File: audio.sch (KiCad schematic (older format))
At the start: 80 parts, among them CN1 LEFT_JOY, CN2 RIGHT_JOY, CN3 RIGHT, CN4 LEFT, Q301 2N3906, Q321 MPF102, Q331 MPF102, U14 LF347, U15 74LS157, U3 PAULA, U38 MC1488

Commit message: Add video power
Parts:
- R401, R408: footprint (none) -> Resistor_THT:R_Axial_DIN0309_L9.0mm_D3.2mm_P15.24mm_Horizontal
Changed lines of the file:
@@
 F 0 "R401" V 6530 1560 50  0000 L CNN
 F 1 "4.7" V 6625 1595 50  0000 L CNN
-F 2 "" V 6555 1660 50  0001 C CNN
+F 2 "Resistor_THT:R_Axial_DIN0309_L9.0mm_D3.2mm_P15.24mm_Horizontal" V 6555 1660 50  0001 C CNN
 F 3 "~" H 6625 1660 50  0001 C CNN
 	1    6625 1660
@@
 F 0 "R408" V 6530 3790 50  0000 L CNN
 F 1 "4.7" V 6625 3825 50  0000 L CNN
-F 2 "" V 6555 3890 50  0001 C CNN
+F 2 "Resistor_THT:R_Axial_DIN0309_L9.0mm_D3.2mm_P15.24mm_Horizontal" V 6555 3890 50  0001 C CNN
 F 3 "~" H 6625 3890 50  0001 C CNN
 	1    6625 3890
@@
 Wire Wire Line
 	5995 5030 7280 5030
-Wire Bus Line
-	1955 4305 1955 4505
-Wire Bus Line
-	1955 6355 1955 7055
-Wire Bus Line
-	1955 4705 1955 6205
 Text Label 1580 4305 0    50   ~ 0
 ipl[0..2]
@@
 Text Label 2130 4605 0    50   ~ 0
 ipl0
+Wire Bus Line
+	1955 4305 1955 4505
+Wire Bus Line
+	1955 6355 1955 7055
+Wire Bus Line
+	1955 4705 1955 6205
 $EndSCHEMATC

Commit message: Add expansion bus
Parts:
- added C3, C301, C302, C305: 330n, symbol Device:C
- added C303, C304: 22u, symbol Device:CP1
- added C306: 10u, symbol Device:CP1
- added C307: 1000u, symbol Device:CP1
- added R301, R302: 10, Raemixx500:R_Axial_DIN0309_L9.0mm_D3.2mm_P12.70mm_Horizontal, symbol Device:R
- added R303, R304: 1k, Raemixx500:R_Axial_DIN0309_L9.0mm_D3.2mm_P12.70mm_Horizontal, symbol Device:R
- added R309: 10, symbol Device:R
- added unit 5 of U14
- added unit 2 of U3
- R305: footprint (none) -> Raemixx500:R_Axial_DIN0309_L9.0mm_D3.2mm_P12.70mm_Horizontal
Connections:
- net labels added: +VDC, -VDC
- net labels removed: VAA
- wire segments 426 -> 477
- no-connect marks 3 -> 4
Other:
- note added: "+VDC (+AV\non original\nschematics) is\npicked up here"
- note added: "-VDC (-AV\non original\nschematics) is\npicked up here"
- note added: "AUDIO POWER"
- note added: "Audio Power\nSupply (+AV/-AV)"
- note added: "PAULA POWER"
- note added: "VAC (VREF\non original\nschematics) is\npicked up here"
- note added: "Vref"
- note removed: "AVref"
- note removed: "Audio Power Supply"
- moved on the sheet: R308, U38A

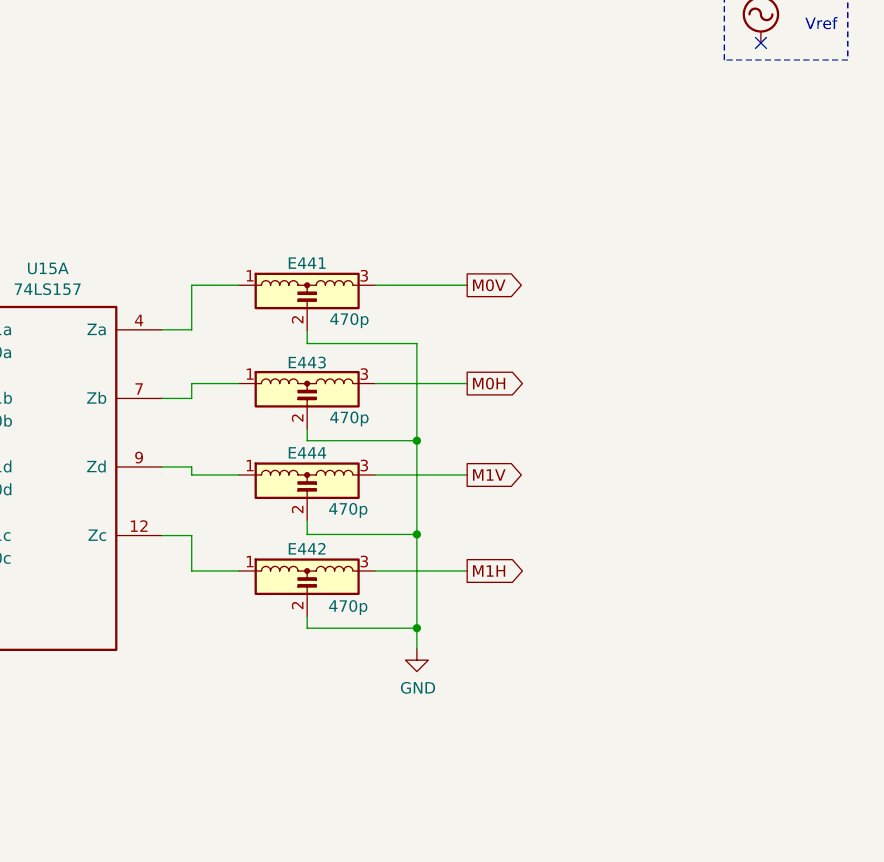
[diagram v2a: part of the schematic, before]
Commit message: Add power & decoupling, not yet complete
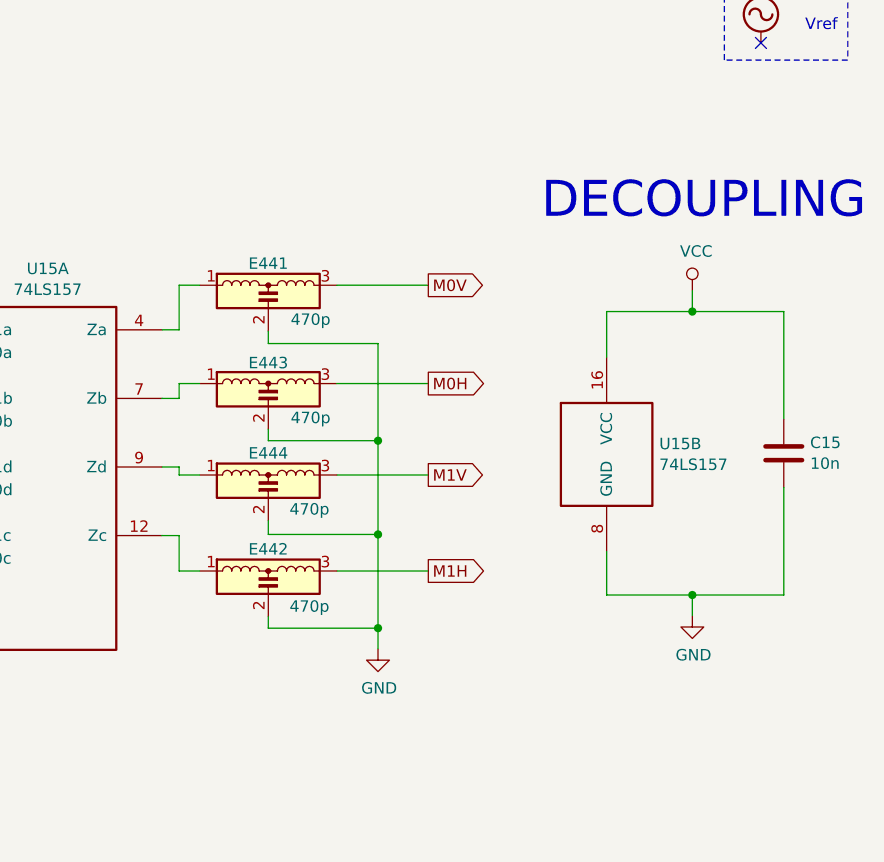
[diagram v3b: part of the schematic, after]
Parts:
- added C15: 10n, symbol Device:C
- added unit 2 of U15
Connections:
- net GND: now also C15.2, U15.8 (GND)
- net VCC: now also C15.1, U15.16 (VCC)
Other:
- note added: "DECOUPLING"
- moved on the sheet: E441, E442, E443, E444
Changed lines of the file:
@@
 $Descr A3 16535 11693
 encoding utf-8
-Sheet 5 11
+Sheet 5 12
 Title "Rämixx500"
 Date "2019-04-16"
@@
 L Device:EMI_Filter_LCL E441
 U 1 1 5D569D5D
-P 13590 2680
-F 0 "E441" H 13590 2875 50  0000 C CNN
-F 1 "470p" H 13775 2630 50  0000 C CNN
-F 2 "" V 13590 2680 50  0001 C CNN
-F 3 "http://www.murata.com/~/media/webrenewal/support/library/catalog/products/emc/emifil/c31e.ashx?la=en-gb" V 13590 2680 50  0001 C CNN
-	1    13590 2680
+P 13420 2680
+F 0 "E441" H 13420 2875 50  0000 C CNN
+F 1 "470p" H 13605 2630 50  0000 C CNN
+F 2 "" V 13420 2680 50  0001 C CNN
+F 3 "http://www.murata.com/~/media/webrenewal/support/library/catalog/products/emc/emifil/c31e.ashx?la=en-gb" V 13420 2680 50  0001 C CNN
+	1    13420 2680
 	1    0    0    -1
 $EndComp
@@
 L Device:EMI_Filter_LCL E443
 U 1 1 5D569D63
-P 13590 3110
-F 0 "E443" H 13590 3300 50  0000 C CNN
-F 1 "470p" H 13775 3060 50  0000 C CNN
-F 2 "" V 13590 3110 50  0001 C CNN
-F 3 "http://www.murata.com/~/media/webrenewal/support/library/catalog/products/emc/emifil/c31e.ashx?la=en-gb" V 13590 3110 50  0001 C CNN
-	1    13590 3110
+P 13420 3110
+F 0 "E443" H 13420 3300 50  0000 C CNN
+F 1 "470p" H 13605 3060 50  0000 C CNN
+F 2 "" V 13420 3110 50  0001 C CNN
+F 3 "http://www.murata.com/~/media/webrenewal/support/library/catalog/products/emc/emifil/c31e.ashx?la=en-gb" V 13420 3110 50  0001 C CNN
+	1    13420 3110
 	1    0    0    -1
 $EndComp
@@
 L Device:EMI_Filter_LCL E444
 U 1 1 5D569D69
-P 13590 3510
-F 0 "E444" H 13590 3705 50  0000 C CNN
-F 1 "470p" H 13770 3460 50  0000 C CNN
-F 2 "" V 13590 3510 50  0001 C CNN
-F 3 "http://www.murata.com/~/media/webrenewal/support/library/catalog/products/emc/emifil/c31e.ashx?la=en-gb" V 13590 3510 50  0001 C CNN
-	1    13590 3510
+P 13420 3510
+F 0 "E444" H 13420 3705 50  0000 C CNN
+F 1 "470p" H 13600 3460 50  0000 C CNN
+F 2 "" V 13420 3510 50  0001 C CNN
+F 3 "http://www.murata.com/~/media/webrenewal/support/library/catalog/products/emc/emifil/c31e.ashx?la=en-gb" V 13420 3510 50  0001 C CNN
+	1    13420 3510
 	1    0    0    -1
 $EndComp
@@
 L Device:EMI_Filter_LCL E442
 U 1 1 5D569D6F
-P 13590 3930
-F 0 "E442" H 13590 4125 50  0000 C CNN
-F 1 "470p" H 13770 3875 50  0000 C CNN
-F 2 "" V 13590 3930 50  0001 C CNN
-F 3 "http://www.murata.com/~/media/webrenewal/support/library/catalog/products/emc/emifil/c31e.ashx?la=en-gb" V 13590 3930 50  0001 C CNN
-	1    13590 3930
-	1    0    0    -1
-$EndComp
-Wire Wire Line
-	13890 2580 14290 2580
-Wire Wire Line
-	13590 2780 13590 2835
-Wire Wire Line
-	13590 2835 14070 2835
-Wire Wire Line
-	14070 2835 14070 3260
-Wire Wire Line
-	13590 3210 13590 3260
-Wire Wire Line
-	13590 3260 14070 3260
-Connection ~ 14070 3260
-Wire Wire Line
-	14070 3260 14070 3670
-Wire Wire Line
-	13590 3610 13590 3670
-Wire Wire Line
-	13590 3670 14070 3670
-Connection ~ 14070 3670
-Wire Wire Line
-	14070 3670 14070 4080
-Wire Wire Line
-	13590 4030 13590 4080
-Wire Wire Line
-	13590 4080 14070 4080
-Connection ~ 14070 4080
-Wire Wire Line
-	14070 4080 14070 4170
+P 13420 3930
+F 0 "E442" H 13420 4125 50  0000 C CNN
+F 1 "470p" H 13600 3875 50  0000 C CNN
+F 2 "" V 13420 3930 50  0001 C CNN
+F 3 "http://www.murata.com/~/media/webrenewal/support/library/catalog/products/emc/emifil/c31e.ashx?la=en-gb" V 13420 3930 50  0001 C CNN
+	1    13420 3930
+	1    0    0    -1
+$EndComp
+Wire Wire Line
+	13720 2580 14120 2580
+Wire Wire Line
+	13420 2780 13420 2835
+Wire Wire Line
+	13420 2835 13900 2835
+Wire Wire Line
+	13900 2835 13900 3260
+Wire Wire Line
+	13420 3210 13420 3260
+Wire Wire Line
+	13420 3260 13900 3260
+Connection ~ 13900 3260
+Wire Wire Line
+	13900 3260 13900 3670
+Wire Wire Line
+	13420 3610 13420 3670
+Wire Wire Line
+	13420 3670 13900 3670
+Connection ~ 13900 3670
+Wire Wire Line
+	13900 3670 13900 4080
+Wire Wire Line
+	13420 4030 13420 4080
+Wire Wire Line
+	13420 4080 13900 4080
+Connection ~ 13900 4080
+Wire Wire Line
+	13900 4080 13900 4170
 $Comp
 L power:GND #PWR0141
 U 1 1 5D569D94
-P 14070 4170
-F 0 "#PWR0141" H 14070 3920 50  0001 C CNN
-F 1 "GND" H 14075 3997 50  0000 C CNN
-F 2 "" H 14070 4170 50  0001 C CNN
-F 3 "" H 14070 4170 50  0001 C CNN
-	1    14070 4170
-	1    0    0    -1
-$EndComp
-Wire Wire Line
-	12955 3075 13085 3075
-Wire Wire Line
-	13085 3075 13085 3010
-Wire Wire Line
-	13085 3010 13290 3010
-Wire Wire Line
-	12955 2775 13085 2775
-Wire Wire Line
-	13085 2775 13085 2580
-Wire Wire Line
-	13085 2580 13290 2580
-Wire Wire Line
-	12955 3375 13085 3375
-Wire Wire Line
-	13085 3375 13085 3410
-Wire Wire Line
-	13085 3410 13290 3410
-Wire Wire Line
-	12955 3675 13085 3675
-Wire Wire Line
-	13085 3675 13085 3830
-Wire Wire Line
-	13085 3830 13290 3830
-Text GLabel 14290 2580 2    50   Output ~ 0
+P 13900 4170
+F 0 "#PWR0141" H 13900 3920 50  0001 C CNN
+F 1 "GND" H 13905 3997 50  0000 C CNN
+F 2 "" H 13900 4170 50  0001 C CNN
+F 3 "" H 13900 4170 50  0001 C CNN
+	1    13900 4170
+	1    0    0    -1
+$EndComp
+Wire Wire Line
+	12955 3075 13030 3075
+Wire Wire Line
+	13030 3075 13030 3010
+Wire Wire Line
+	13030 3010 13120 3010
+Wire Wire Line
+	12955 2775 13030 2775
+Wire Wire Line
+	13030 2775 13030 2580
+Wire Wire Line
+	13030 2580 13120 2580
+Wire Wire Line
+	12955 3375 13030 3375
+Wire Wire Line
+	13030 3375 13030 3410
+Wire Wire Line
+	13030 3410 13120 3410
+Wire Wire Line
+	12955 3675 13030 3675
+Wire Wire Line
+	13030 3675 13030 3830
+Wire Wire Line
+	13030 3830 13120 3830
+Text GLabel 14120 2580 2    50   Output ~ 0
 M0V
 Wire Wire Line
-	13890 3010 14290 3010
-Text GLabel 14290 3010 2    50   Output ~ 0
+	13720 3010 14120 3010
+Text GLabel 14120 3010 2    50   Output ~ 0
 M0H
 Wire Wire Line
-	13890 3410 14290 3410
-Text GLabel 14290 3410 2    50   Output ~ 0
+	13720 3410 14120 3410
+Text GLabel 14120 3410 2    50   Output ~ 0
 M1V
 Wire Wire Line
-	13890 3830 14290 3830
-Text GLabel 14290 3830 2    50   Output ~ 0
+	13720 3830 14120 3830
+Text GLabel 14120 3830 2    50   Output ~ 0
 M1H
 $Comp
@@
 Text Notes 525  11075 0    315  ~ 0
 AUDIO POWER
+$Comp
+L 74ls157:74LS157 U15
+U 2 1 5EC4854E
+P 14900 3345
+F 0 "U15" H 15130 3416 50  0000 L CNN
+F 1 "74LS157" H 15130 3325 50  0000 L CNN
+F 2 "Package_DIP:DIP-16_W7.62mm_Socket_LongPads" H 14900 3345 50  0001 C CNN
+F 3 "http://www.ti.com/lit/gpn/sn74LS157" H 14900 3345 50  0001 C CNN
+	2    14900 3345
+	1    0    0    -1
+$EndComp
+$Comp
+L Device:C C15
+U 1 1 5EC8858D
+P 15675 3315
+F 0 "C15" H 15790 3361 50  0000 L CNN
+F 1 "10n" H 15790 3270 50  0000 L CNN
+F 2 "" H 15713 3165 50  0001 C CNN
+F 3 "~" H 15675 3315 50  0001 C CNN
+	1    15675 3315
+	1    0    0    -1
+$EndComp
+Wire Wire Line
+	14900 2895 14900 2695
+Wire Wire Line
+	14900 2695 15275 2695
+Wire Wire Line
+	15675 2695 15675 3165
+Wire Wire Line
+	15675 3465 15675 3935
+Wire Wire Line
+	15675 3935 15275 3935
+Wire Wire Line
+	14900 3935 14900 3745
+Wire Wire Line
+	15275 3935 15275 4025
+$Comp
+L power:GND #PWR0222
+U 1 1 5ED09E51
+P 15275 4025
+F 0 "#PWR0222" H 15275 3775 50  0001 C CNN
+F 1 "GND" H 15280 3852 50  0000 C CNN
+F 2 "" H 15275 4025 50  0001 C CNN
+F 3 "" H 15275 4025 50  0001 C CNN
+	1    15275 4025
+	1    0    0    -1
+$EndComp
+Connection ~ 15275 3935
+Wire Wire Line
+	15275 3935 14900 3935
+$Comp
+L power:VCC #PWR0223
+U 1 1 5ED4B558
+P 15275 2605
+F 0 "#PWR0223" H 15275 2455 50  0001 C CNN
+F 1 "VCC" H 15292 2778 50  0000 C CNN
+F 2 "" H 15275 2605 50  0001 C CNN
+F 3 "" H 15275 2605 50  0001 C CNN
+	1    15275 2605
+	1    0    0    -1
+$EndComp
+Wire Wire Line
+	15275 2605 15275 2695
+Connection ~ 15275 2695
+Wire Wire Line
+	15275 2695 15675 2695
 Wire Bus Line
 	1955 4305 1955 4505
@@
 Wire Bus Line
 	1955 4705 1955 6205
+Text Notes 16035 2305 2    157  ~ 0
+DECOUPLING
 $EndSCHEMATC

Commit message: Add RTC
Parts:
- C303, C304: footprint (none) -> Capacitor_THT:CP_Radial_D5.0mm_P2.00mm
- C306, C307, C324, C334: footprint (none) -> Capacitor_THT:CP_Radial_D8.0mm_P5.00mm
- CN3: footprint (none) -> w_conn_av:rca_red
- CN4: footprint (none) -> w_conn_av:rca_white
- JP10A1, JP10B1: footprint Jumper:SolderJumper-2_P1.3mm_Bridged_RoundedPad1.0x1.5mm -> Raemixx500:Jumper2-Bridged
- JP8: footprint (none) -> Raemixx500:Jumper3-Bridged23
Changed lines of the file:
@@
 $Descr A3 16535 11693
 encoding utf-8
-Sheet 5 12
+Sheet 5 13
 Title "Rämixx500"
 Date "2019-04-16"
@@
 F 0 "JP8" V 5645 2507 50  0000 L CNN
 F 1 "Jumper_3_Bridged23" V 5690 2507 50  0001 L CNN
-F 2 "" H 5645 2440 50  0001 C CNN
+F 2 "Raemixx500:Jumper3-Bridged23" H 5645 2440 50  0001 C CNN
 F 3 "~" H 5645 2440 50  0001 C CNN
 	1    5645 2440
@@
 F 0 "C324" V 10525 8860 50  0000 C CNN
 F 1 "22u" V 10405 8885 50  0000 C CNN
-F 2 "" H 10475 9035 50  0001 C CNN
+F 2 "Capacitor_THT:CP_Radial_D8.0mm_P5.00mm" H 10475 9035 50  0001 C CNN
 F 3 "~" H 10475 9035 50  0001 C CNN
 	1    10475 9035
@@
 F 0 "CN4" H 12965 8891 50  0000 L CNN
 F 1 "LEFT" H 12965 8800 50  0000 L CNN
-F 2 "" H 12865 8915 50  0001 C CNN
+F 2 "w_conn_av:rca_white" H 12865 8915 50  0001 C CNN
 F 3 " ~" H 12865 8915 50  0001 C CNN
 	1    12865 8915
@@
 F 0 "C334" V 10525 7065 50  0000 C CNN
 F 1 "22u" V 10405 7090 50  0000 C CNN
-F 2 "" H 10475 7240 50  0001 C CNN
+F 2 "Capacitor_THT:CP_Radial_D8.0mm_P5.00mm" H 10475 7240 50  0001 C CNN
 F 3 "~" H 10475 7240 50  0001 C CNN
 	1    10475 7240
@@
 F 0 "CN3" H 12964 7096 50  0000 L CNN
 F 1 "RIGHT" H 12964 7005 50  0000 L CNN
-F 2 "" H 12865 7120 50  0001 C CNN
+F 2 "w_conn_av:rca_red" H 12865 7120 50  0001 C CNN
 F 3 " ~" H 12865 7120 50  0001 C CNN
 	1    12865 7120
@@
 F 0 "JP10B1" H 11260 8543 50  0000 C CNN
 F 1 "Jumper_2_Bridged" H 11260 8544 50  0001 C CNN
-F 2 "Jumper:SolderJumper-2_P1.3mm_Bridged_RoundedPad1.0x1.5mm" H 11260 8440 50  0001 C CNN
+F 2 "Raemixx500:Jumper2-Bridged" H 11260 8440 50  0001 C CNN
 F 3 "~" H 11260 8440 50  0001 C CNN
 	1    11260 8440
@@
 F 0 "JP10A1" H 6150 6558 50  0000 C CNN
 F 1 "Jumper_2_Bridged" H 6150 6559 50  0001 C CNN
-F 2 "Jumper:SolderJumper-2_P1.3mm_Bridged_RoundedPad1.0x1.5mm" H 6150 6455 50  0001 C CNN
+F 2 "Raemixx500:Jumper2-Bridged" H 6150 6455 50  0001 C CNN
 F 3 "~" H 6150 6455 50  0001 C CNN
 	1    6150 6455
@@
 F 0 "C307" H 2360 2161 50  0000 L CNN
 F 1 "1000u" H 2360 2070 50  0000 L CNN
-F 2 "" H 2245 2115 50  0001 C CNN
+F 2 "Capacitor_THT:CP_Radial_D8.0mm_P5.00mm" H 2245 2115 50  0001 C CNN
 F 3 "~" H 2245 2115 50  0001 C CNN
 	1    2245 2115
@@
 F 0 "C306" H 4380 2161 50  0000 L CNN
 F 1 "10u" H 4380 2070 50  0000 L CNN
-F 2 "" H 4265 2115 50  0001 C CNN
+F 2 "Capacitor_THT:CP_Radial_D8.0mm_P5.00mm" H 4265 2115 50  0001 C CNN
 F 3 "~" H 4265 2115 50  0001 C CNN
 	1    4265 2115
@@
 F 0 "C303" H 2175 9561 50  0000 L CNN
 F 1 "22u" H 2175 9470 50  0000 L CNN
-F 2 "" H 2060 9515 50  0001 C CNN
+F 2 "Capacitor_THT:CP_Radial_D5.0mm_P2.00mm" H 2060 9515 50  0001 C CNN
 F 3 "~" H 2060 9515 50  0001 C CNN
 	1    2060 9515
@@
 F 0 "C304" H 2175 9946 50  0000 L CNN
 F 1 "22u" H 2175 9855 50  0000 L CNN
-F 2 "" H 2060 9900 50  0001 C CNN
+F 2 "Capacitor_THT:CP_Radial_D5.0mm_P2.00mm" H 2060 9900 50  0001 C CNN
 F 3 "~" H 2060 9900 50  0001 C CNN
 	1    2060 9900

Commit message: Fix power-up reset
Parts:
- C15, C3: footprint (none) -> Raemixx500:C_Axial_L6.3mm_D2.5mm_P10.16mm
- Q301, Q321, Q331: footprint (none) -> Package_TO_SOT_THT:TO-92L_Inline_Wide
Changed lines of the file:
@@
 EESchema Schematic File Version 4
 LIBS:Raemix500-cache
-EELAYER 26 0
+EELAYER 29 0
 EELAYER END
 $Descr A3 16535 11693
@@
 F 0 "Q321" V 8913 9325 50  0000 C CNN
 F 1 "MPF102" V 8822 9325 50  0000 C CNN
-F 2 "" H 8785 9425 50  0001 C CNN
+F 2 "Package_TO_SOT_THT:TO-92L_Inline_Wide" H 8785 9425 50  0001 C CNN
 F 3 "~" H 8585 9325 50  0001 C CNN
 	1    8585 9325
@@
 F 0 "Q331" V 8913 7530 50  0000 C CNN
 F 1 "MPF102" V 8822 7530 50  0000 C CNN
-F 2 "" H 8785 7630 50  0001 C CNN
+F 2 "Package_TO_SOT_THT:TO-92L_Inline_Wide" H 8785 7630 50  0001 C CNN
 F 3 "~" H 8585 7530 50  0001 C CNN
 	1    8585 7530
@@
 F 0 "Q301" H 5226 9239 50  0000 L CNN
 F 1 "2N3906" H 5226 9330 50  0000 L CNN
-F 2 "" H 5235 9385 50  0001 C CNN
+F 2 "Package_TO_SOT_THT:TO-92L_Inline_Wide" H 5235 9385 50  0001 C CNN
 F 3 "~" H 5035 9285 50  0001 C CNN
 	1    5035 9285
@@
 F 0 "C3" H 1940 2161 50  0000 L CNN
 F 1 "330n" H 1940 2070 50  0000 L CNN
-F 2 "" H 1863 1965 50  0001 C CNN
+F 2 "Raemixx500:C_Axial_L6.3mm_D2.5mm_P10.16mm" H 1863 1965 50  0001 C CNN
 F 3 "~" H 1825 2115 50  0001 C CNN
 	1    1825 2115
@@
 F 0 "C15" H 15790 3361 50  0000 L CNN
 F 1 "10n" H 15790 3270 50  0000 L CNN
-F 2 "" H 15713 3165 50  0001 C CNN
+F 2 "Raemixx500:C_Axial_L6.3mm_D2.5mm_P10.16mm" H 15713 3165 50  0001 C CNN
 F 3 "~" H 15675 3315 50  0001 C CNN
 	1    15675 3315

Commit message: Work in progress
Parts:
- C301, C302, C305, C308, C321, C322, C323, C331, C332, C333, C411, C412, C413, C421, C422, C423: footprint (none) -> Raemixx500:C_Axial_L9.0mm_D3.2mm_P12.70mm
- E305, E306, E401, E408, E411, E412, E413, E414, E415, E416, E417, E421, E422, E423, E424, E425, E426, E427, E441, E442, E443, E444: footprint (none) -> Raemixx500:EMI_Filter_Long
- R306, R307, R308, R321, R322, R323, R326, R331, R332, R333, R336, R339: footprint (none) -> Raemixx500:R_Axial_DIN0309_L9.0mm_D3.2mm_P12.70mm_Horizontal
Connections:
- net at CN1.4: now also E414.3; no longer E414.1
- net at RP401.6 (R5), U15.5 (I0b): now also E414.1; no longer E414.3
